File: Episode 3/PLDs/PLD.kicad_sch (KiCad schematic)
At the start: 16 parts, among them SW2 PAUSE, U10 74HCT74, U11 ATF22V10, U7 ATF22V10C, U8 ATF750C, U9 74AHCT14, X1 16MHz

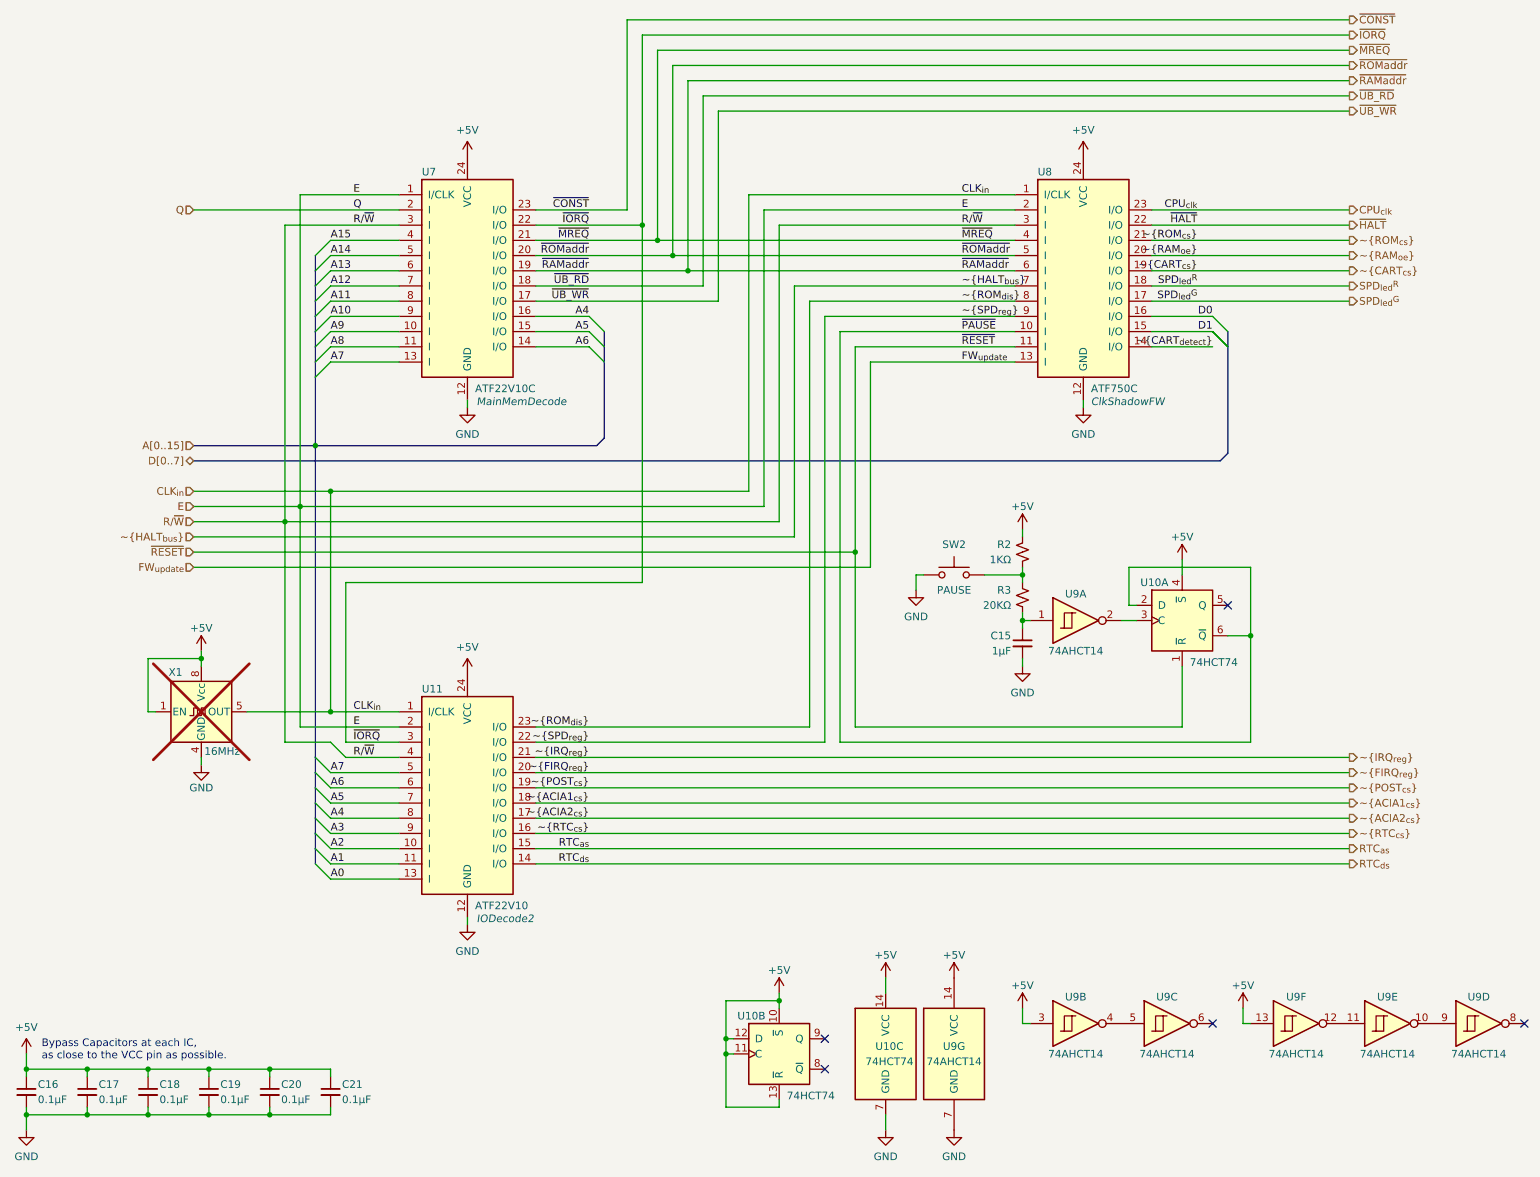
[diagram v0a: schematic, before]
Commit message: Updating PLD pin  assignments
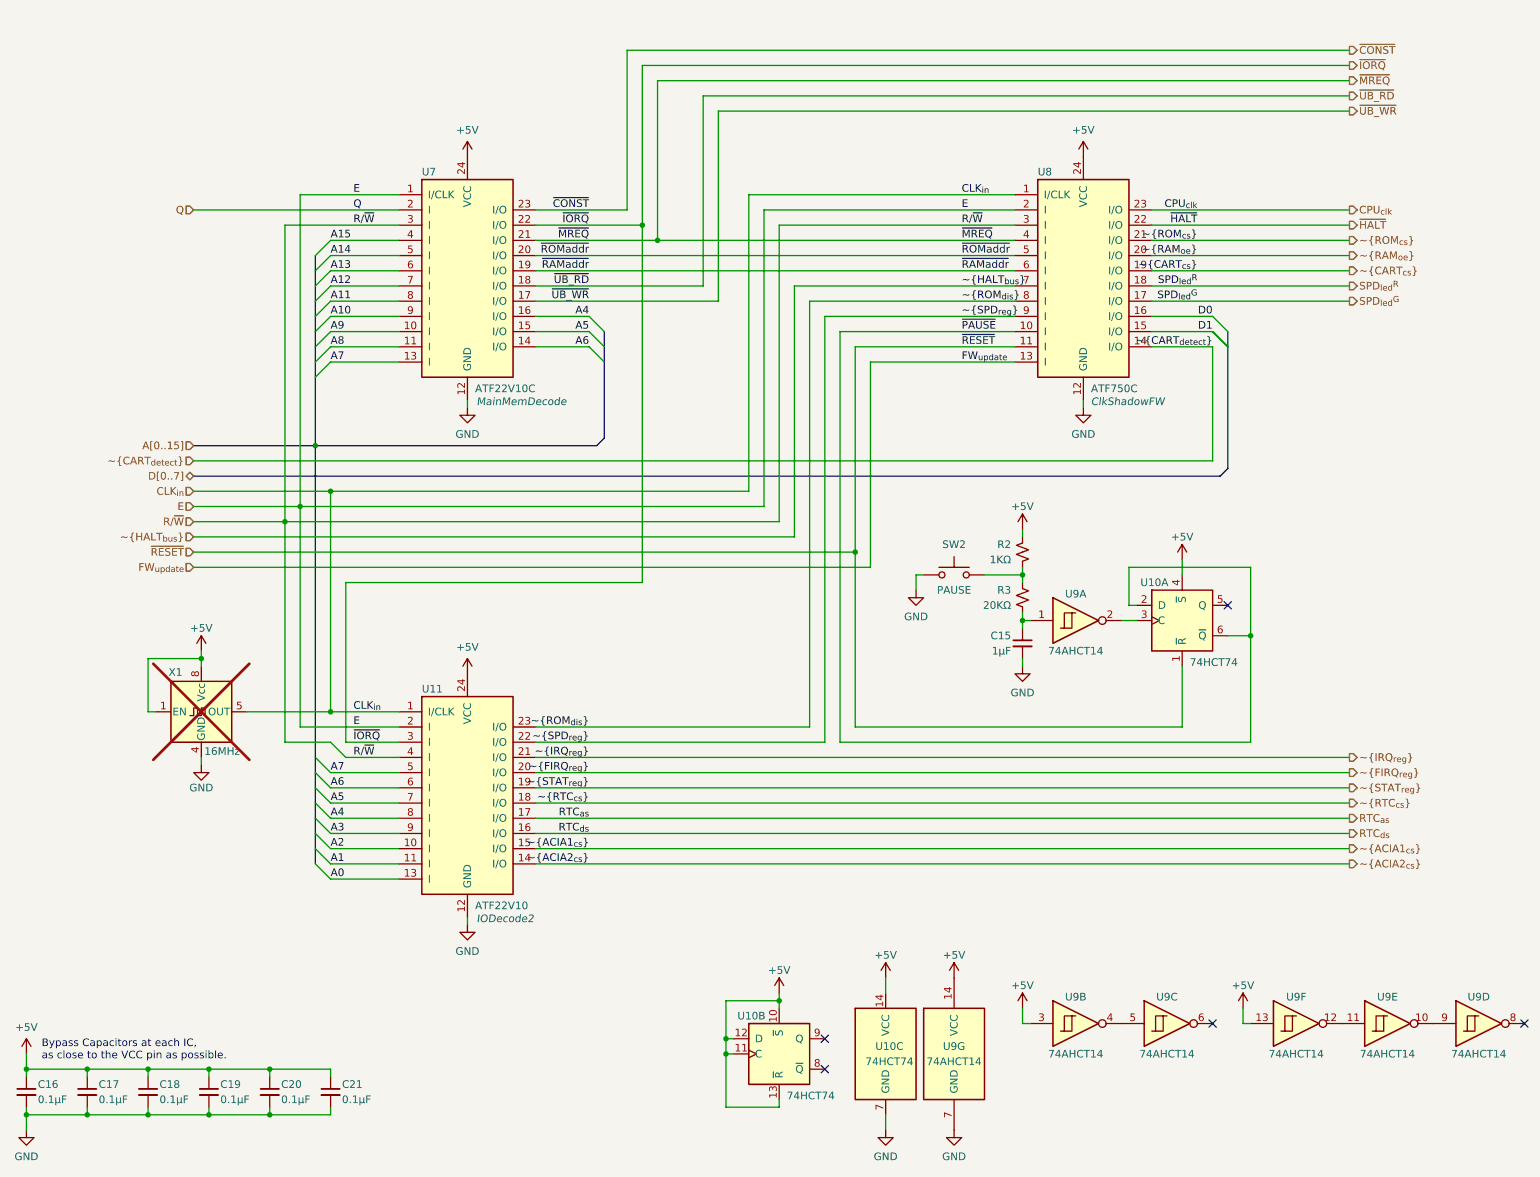
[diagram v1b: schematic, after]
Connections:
- net RTC_{as}: now also U11.17 (I/O); no longer U11.15 (I/O)
- net RTC_{ds}: now also U11.16 (I/O); no longer U11.14 (I/O)
- net ~{ACIA1_{cs}}: now also U11.15 (I/O); no longer U11.18 (I/O)
- net ~{ACIA2_{cs}}: now also U11.14 (I/O); no longer U11.17 (I/O)
- net ~{RTC_{cs}}: now also U11.18 (I/O); no longer U11.16 (I/O)
- net ~{POST_{cs}} renamed ~{STAT_{reg}}
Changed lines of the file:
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@@
 	)
 	(junction
-		(at 120.65 53.34)
-		(diameter 0)
-		(color 0 0 0 0)
-	)
-	(junction
 		(at 33.02 189.23)
 		(diameter 0)
@@
 	)
 	(junction
-		(at 123.19 55.88)
-		(diameter 0)
-		(color 0 0 0 0)
-	)
-	(junction
 		(at 129.54 186.69)
 		(diameter 0)
@@
 	(bus
 		(pts
-			(xy 40.64 87.63) (xy 212.09 87.63)
+			(xy 40.64 90.17) (xy 212.09 90.17)
 		)
 		(stroke
@@
 		)
 	)
-	(wire
-		(pts
-			(xy 123.19 24.13) (xy 123.19 55.88)
-		)
-		(stroke
-			(width 0)
-			(type default)
-		)
-	)
 	(bus
 		(pts
@@
 	(wire
 		(pts
-			(xy 118.11 19.05) (xy 233.68 19.05)
+			(xy 118.11 24.13) (xy 233.68 24.13)
 		)
 		(stroke
@@
 	(wire
 		(pts
-			(xy 97.79 55.88) (xy 123.19 55.88)
-		)
-		(stroke
-			(width 0)
-			(type default)
-		)
-	)
-	(wire
-		(pts
 			(xy 129.54 184.15) (xy 129.54 186.69)
 		)
@@
 	(wire
 		(pts
-			(xy 118.11 19.05) (xy 118.11 50.8)
+			(xy 118.11 24.13) (xy 118.11 50.8)
 		)
 		(stroke
@@
 	(wire
 		(pts
-			(xy 120.65 53.34) (xy 177.8 53.34)
+			(xy 97.79 53.34) (xy 177.8 53.34)
 		)
 		(stroke
@@
 		)
 	)
-	(wire
-		(pts
-			(xy 120.65 21.59) (xy 233.68 21.59)
-		)
-		(stroke
-			(width 0)
-			(type default)
-		)
-	)
 	(bus
 		(pts
@@
 	(wire
 		(pts
-			(xy 123.19 55.88) (xy 177.8 55.88)
+			(xy 97.79 55.88) (xy 177.8 55.88)
 		)
 		(stroke
@@
 	(wire
 		(pts
-			(xy 113.03 13.97) (xy 113.03 45.72)
+			(xy 113.03 19.05) (xy 113.03 45.72)
 		)
 		(stroke
@@
 	(bus
 		(pts
-			(xy 212.09 87.63) (xy 213.36 86.36)
+			(xy 212.09 90.17) (xy 213.36 88.9)
 		)
 		(stroke
@@
 	(wire
 		(pts
-			(xy 120.65 21.59) (xy 120.65 53.34)
-		)
-		(stroke
-			(width 0)
-			(type default)
-		)
-	)
-	(wire
-		(pts
 			(xy 63.5 134.62) (xy 66.04 137.16)
 		)
@@
 	(bus
 		(pts
-			(xy 213.36 68.58) (xy 213.36 86.36)
+			(xy 213.36 68.58) (xy 213.36 88.9)
 		)
 		(stroke
@@
 	(wire
 		(pts
-			(xy 113.03 13.97) (xy 233.68 13.97)
+			(xy 113.03 19.05) (xy 233.68 19.05)
 		)
 		(stroke
@@
 	(wire
 		(pts
-			(xy 115.57 16.51) (xy 115.57 48.26)
+			(xy 115.57 21.59) (xy 115.57 48.26)
 		)
 		(stroke
@@
 	(wire
 		(pts
-			(xy 115.57 16.51) (xy 233.68 16.51)
+			(xy 115.57 21.59) (xy 233.68 21.59)
 		)
 		(stroke
@@
 	(wire
 		(pts
-			(xy 97.79 53.34) (xy 120.65 53.34)
-		)
-		(stroke
-			(width 0)
-			(type default)
-		)
-	)
-	(wire
-		(pts
 			(xy 213.36 116.84) (xy 217.17 116.84)
 		)
@@
 		)
 	)
+	(wire
+		(pts
+			(xy 210.82 68.58) (xy 210.82 87.63)
+		)
+		(stroke
+			(width 0)
+			(type default)
+		)
+	)
 	(bus
 		(pts
@@
 	(wire
 		(pts
-			(xy 86.36 78.74) (xy 86.36 77.47)
+			(xy 40.64 87.63) (xy 210.82 87.63)
 		)
 		(stroke
@@
 	(wire
 		(pts
-			(xy 66.04 107.95) (xy 115.57 107.95)
+			(xy 86.36 78.74) (xy 86.36 77.47)
 		)
 		(stroke
@@
 		)
 	)
-	(bus
+	(wire
 		(pts
-			(xy 60.96 142.24) (xy 60.96 139.7)
+			(xy 66.04 107.95) (xy 115.57 107.95)
 		)
 		(stroke
@@
 		)
 	)
-	(wire
+	(bus
 		(pts
-			(xy 63.5 92.71) (xy 63.5 129.54)
+			(xy 60.96 142.24) (xy 60.96 139.7)
 		)
 		(stroke
@@
 	(wire
 		(pts
-			(xy 58.42 132.08) (xy 74.93 132.08)
+			(xy 63.5 92.71) (xy 63.5 129.54)
 		)
 		(stroke
@@
 	(wire
 		(pts
-			(xy 133.35 43.18) (xy 133.35 92.71)
+			(xy 58.42 132.08) (xy 74.93 132.08)
 		)
 		(stroke
@@
 	(wire
 		(pts
-			(xy 123.19 24.13) (xy 233.68 24.13)
+			(xy 133.35 43.18) (xy 133.35 92.71)
 		)
 		(stroke
@@
 	)
 	(label "RTC_{ds}"
-		(at 106.68 154.94 180)
+		(at 106.68 149.86 180)
 		(effects
 			(font
@@
 	)
 	(label "RTC_{as}"
-		(at 106.68 152.4 180)
+		(at 106.68 147.32 180)
 		(effects
 			(font
@@
 		)
 	)
+	(label "~{STAT_{reg}}"
+		(at 106.68 142.24 180)
+		(effects
+			(font
+				(size 1.27 1.27)
+			)
+			(justify right bottom)
+		)
+	)
 	(label "~{SPD_{reg}}"
 		(at 106.68 134.62 180)
@@
 	)
 	(label "~{ACIA2_{cs}}"
-		(at 106.68 147.32 180)
+		(at 106.68 154.94 180)
 		(effects
 			(font
@@
 	)
 	(label "~{RTC_{cs}}"
-		(at 106.68 149.86 180)
+		(at 106.68 144.78 180)
 		(effects
 			(font
@@
 	)
 	(label "~{ACIA1_{cs}}"
-		(at 106.68 144.78 180)
+		(at 106.68 152.4 180)
 		(effects
 			(font
@@
 		)
 	)
-	(label "~{POST_{cs}}"
-		(at 106.68 142.24 180)
-		(effects
-			(font
-				(size 1.27 1.27)
-			)
-			(justify right bottom)
-		)
-	)
 	(label "CPU_{clk}"
 		(at 208.28 45.72 180)
@@
 		)
 	)
-	(hierarchical_label "RTC_{as}"
+	(hierarchical_label "~{ACIA1_{cs}}"
 		(shape output)
 		(at 233.68 152.4 0)
@@
 		)
 	)
-	(hierarchical_label "~{ACIA2_{cs}}"
-		(shape output)
-		(at 233.68 147.32 0)
-		(effects
-			(font
-				(size 1.27 1.27)
-			)
-			(justify left)
-		)
-	)
-	(hierarchical_label "~{POST_{cs}}"
-		(shape output)
-		(at 233.68 142.24 0)
-		(effects
-			(font
-				(size 1.27 1.27)
-			)
-			(justify left)
-		)
-	)
-	(hierarchical_label "~{ACIA1_{cs}}"
+	(hierarchical_label "~{RTC_{cs}}"
 		(shape output)
 		(at 233.68 144.78 0)
@@
 		)
 	)
-	(hierarchical_label "~{RAMaddr}"
+	(hierarchical_label "RTC_{as}"
 		(shape output)
-		(at 233.68 24.13 0)
+		(at 233.68 147.32 0)
 		(effects
 			(font
@@
 		)
 	)
-	(hierarchical_label "~{ROMaddr}"
+	(hierarchical_label "~{STAT_{reg}}"
 		(shape output)
-		(at 233.68 21.59 0)
+		(at 233.68 142.24 0)
 		(effects
 			(font
@@
 		)
 	)
-	(hierarchical_label "~{CART_{cs}}"
+	(hierarchical_label "RTC_{ds}"
 		(shape output)
-		(at 233.68 55.88 0)
+		(at 233.68 149.86 0)
 		(effects
 			(font
@@
 		)
 	)
-	(hierarchical_label "~{RAM_{oe}}"
+	(hierarchical_label "~{CART_{cs}}"
 		(shape output)
-		(at 233.68 53.34 0)
+		(at 233.68 55.88 0)
 		(effects
 			(font
@@
 		)
 	)
-	(hierarchical_label "~{CONST}"
+	(hierarchical_label "~{RAM_{oe}}"
 		(shape output)
-		(at 233.68 13.97 0)
+		(at 233.68 53.34 0)
 		(effects
 			(font
@@
 		)
 	)
-	(hierarchical_label "RTC_{ds}"
+	(hierarchical_label "~{CONST}"
 		(shape output)
-		(at 233.68 154.94 0)
+		(at 233.68 19.05 0)
 		(effects
 			(font
@@
 	(hierarchical_label "~{MREQ}"
 		(shape output)
-		(at 233.68 19.05 0)
+		(at 233.68 24.13 0)
 		(effects
 			(font
@@
 		)
 	)
-	(hierarchical_label "~{RTC_{cs}}"
-		(shape output)
-		(at 233.68 149.86 0)
-		(effects
-			(font
-				(size 1.27 1.27)
-			)
-			(justify left)
-		)
-	)
 	(hierarchical_label "~{HALT_{bus}}"
 		(shape input)
@@
 		)
 	)
+	(hierarchical_label "~{CART_{detect}}"
+		(shape input)
+		(at 40.64 87.63 180)
+		(effects
+			(font
+				(size 1.27 1.27)
+			)
+			(justify right)
+		)
+	)
 	(hierarchical_label "~{RESET}"
 		(shape input)
@@
 		)
 	)
+	(hierarchical_label "~{ACIA2_{cs}}"
+		(shape output)
+		(at 233.68 154.94 0)
+		(effects
+			(font
+				(size 1.27 1.27)
+			)
+			(justify left)
+		)
+	)
 	(hierarchical_label "~{IORQ}"
 		(shape output)
-		(at 233.68 16.51 0)
+		(at 233.68 21.59 0)
 		(effects
 			(font
@@
 	(hierarchical_label "D[0..7]"
 		(shape bidirectional)
-		(at 40.64 87.63 180)
+		(at 40.64 90.17 180)
 		(effects
 			(font
